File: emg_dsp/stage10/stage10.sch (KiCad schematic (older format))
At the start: 210 parts, among them U1 RS232_CON, U10 EN_VDD, U11 USBLC6, U12 ABM10XTAL-24, U13 BF527, U14 MIC5365, U15 SST25VF040B, U16 ADSP_JTAG_CON, U17 LAN8710A, U18 74LCX541, U19 SFE-MAGJACK, U2 VEE, U20 MAX6711Z, U21 TESTCON, U22 74LCX541, U23 74LCX541, U24 NRF24L01-BREAK, U25 NRF24L01-BREAK, U26 NRF24L01-BREAK, U3 ADM3202, U4 TPS62410, U5 GT12MABE, U6 FCI_USB_B, U7 MT48LC16M16A2, U8 EN_VCC, U9 ABM10XTAL-25

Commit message: working on new (final?) headstage/bridge. added power-over-ethernet to the bridge, as well as programming and debug for the headstage. want to put an LCD on there too...
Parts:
- removed R38, R39: 200, 0402, symbol R
- removed TP38, TP39, TP40, TP41: TP, 2.9mm_hole, symbol TP
- removed TP5: TWI_SCL, TP, symbol TP
- removed TP6: TWI_SDA, TP, symbol TP
- removed U19: SFE-MAGJACK, SFE-MAGJACK, symbol SFE-MAGJACK
- added C?: 100pf, 0402, symbol C
- added C?: 0.1uf, 0402, symbol C
- added C? (x2): 1uf, 0402, symbol C
- added R?: 130, 0402, symbol R
- added R? (x3): 200, 0402, symbol R
- added R? (x4): 10k, 0402, symbol R
- added U?: POE-JACK, POE-JACK, symbol POE-JACK
- added U?: TESTCON, 7x100mil, symbol TESTCON
- added U?: 74LCX541, TSSOP-20, symbol 74LCX541
- added U? (x2): 9X100, omnetics_9, symbol 9X100
- added U?: ADSP_JTAG_CON, 7x2x100, symbol ADSP_JTAG_CON
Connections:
- net labels added: VBUS
- wire segments 570 -> 636
- no-connect marks 25 -> 30
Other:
- note added: "MISO"
- note added: "MOSI"
- note added: "MR"
- note added: "PF2"
- note added: "SCK"
- note added: "TCK"
- note added: "TDI"
- note added: "TDO"
- note added: "TMS"
- note added: "_emu"
- note added: "_trst"
- note added: "this for debugging the headstage."
- note added: "this for programming the headstage."
- moved on the sheet: C48

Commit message: word, schematics for 9/10 are close to done. start changing the boards...
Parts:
- removed D10, D11, D12, D13, D14, D15, D16, D2, D3, D4, D5, D6, D7, D8, D9: LED, 0603, symbol LED
- removed R? (x2): 10k, 0402, symbol R
- added C74, C77: 47pf, 0402, symbol C
- added C91: 1uf, 0402, symbol C
- added D22, D23, D24, D25, D26, D27, D28, D29, D30, D31, D32, D33, D34, D35, D36: 475-2558, D0603, symbol LED
- added R132, R133: 33, 0402, symbol R
- added U42: NHD-0216KZW, NHD-0216KZW, symbol NHD-0216KZW
- D1: value LED -> 475-2558; footprint 0603 -> D0603
- R113: renamed from R?; value 10k -> 22k
- R57, R58, R59, R60, R61, R62, R63, R64, R65, R66, R67, R68, R69, R70, R71, R72: value 130 -> 200
- TP11: value NRF_CSN -> PF0-DR0PRI
- TP12: value NRF_CE -> PF7-DR0SEC
- TP13: value NRF_IRQ -> PF1-RFS0
- TP14: value WIRED_STEP -> PF2-RSCLK
- gave numbers to parts that had none: 15
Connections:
- net GND: now also C74.2, C77.2, C91.1, U42.1 (Vss), U42.10 (DB3), U42.11 (DB4), U42.15 (NC), U42.3 (NC), U42.4 (RS), U42.5 (R/W), U42.6 (E), U42.7 (DB0), U42.8 (DB1), U42.9 (DB2)
- net VDD: now also C91.2, U42.2 (Vdd)
- net at TP18.1, U23.15 (Y4): now also D28.1 (A)
- net at R64.1: now also D28.2 (K)
- net at TP21.1, U23.12 (Y7): now also D34.1 (A)
- net at R70.1: now also D34.2 (K)
- net at TP22.1, U23.11 (Y8): now also D36.1 (A)
- net at R72.1: now also D36.2 (K)
- net at TP17.1, U23.16 (Y3): now also D26.1 (A)
- net at TP16.1, U23.17 (Y2): now also D24.1 (A)
- net at TP8.1, U22.17 (Y2): now also D23.1 (A)
- net at TP9.1, U22.16 (Y3): now also D25.1 (A)
- net at TP10.1, U22.15 (Y4): now also D27.1 (A)
- net at TP11.1, U22.14 (Y5): now also D29.1 (A)
- net at TP12.1, U22.13 (Y6): now also D31.1 (A)
- net at TP14.1, U22.11 (Y8): now also D35.1 (A)
- net at R71.1: now also D35.2 (K)
- net at R67.1: now also D31.2 (K)
- net at R65.1: now also D29.2 (K)
- net at R63.1: now also D27.2 (K)
- net LCD_SDI: now reaches U13.J1 (PG11)
- net LCD_SDI: now also U42.14 (SDI)
- net at U13.J2 (PG12): now also R133.1
- net at U13.K1 (PG9-TACI5): now also R132.1
- net LCD_SDO: now reaches U13.K2 (PG10-TACI6)
- net LCD_SDO: now also U42.13 (SDO)
- net at U18.2 (A1), U21.3 (_cs): now also C77.1
- net at TP15.1, U23.18 (Y1): now also D22.1 (A)
- net at R58.1: now also D22.2 (K)
- net at R60.1: now also D24.2 (K)
- net at R62.1: now also D26.2 (K)
- net at TP20.1, U23.13 (Y6): now also D32.1 (A)
- net at TP19.1, U23.14 (Y5): now also D30.1 (A)
- net at R66.1: now also D30.2 (K)
- net at R68.1: now also D32.2 (K)
- net at TP13.1, U22.12 (Y7): now also D33.1 (A)
- net at R69.1: now also D33.2 (K)
- net at R61.1: now also D25.2 (K)
- net at R59.1: now also D23.2 (K)
- net at U33.2 (A1), U35.3 (_cs): now also C74.1
- new net LCD_CS: R133.2, U42.16 (_cs)
- new net LCD_SCL: R132.2, U42.12 (SCL)
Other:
- note added: "emu pulled hi\ntrst pulled low\non 'stage"
- moved on the sheet: C55, C56, D1, R42, R43, R44, R45, R46, R47, R48, R49, R57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

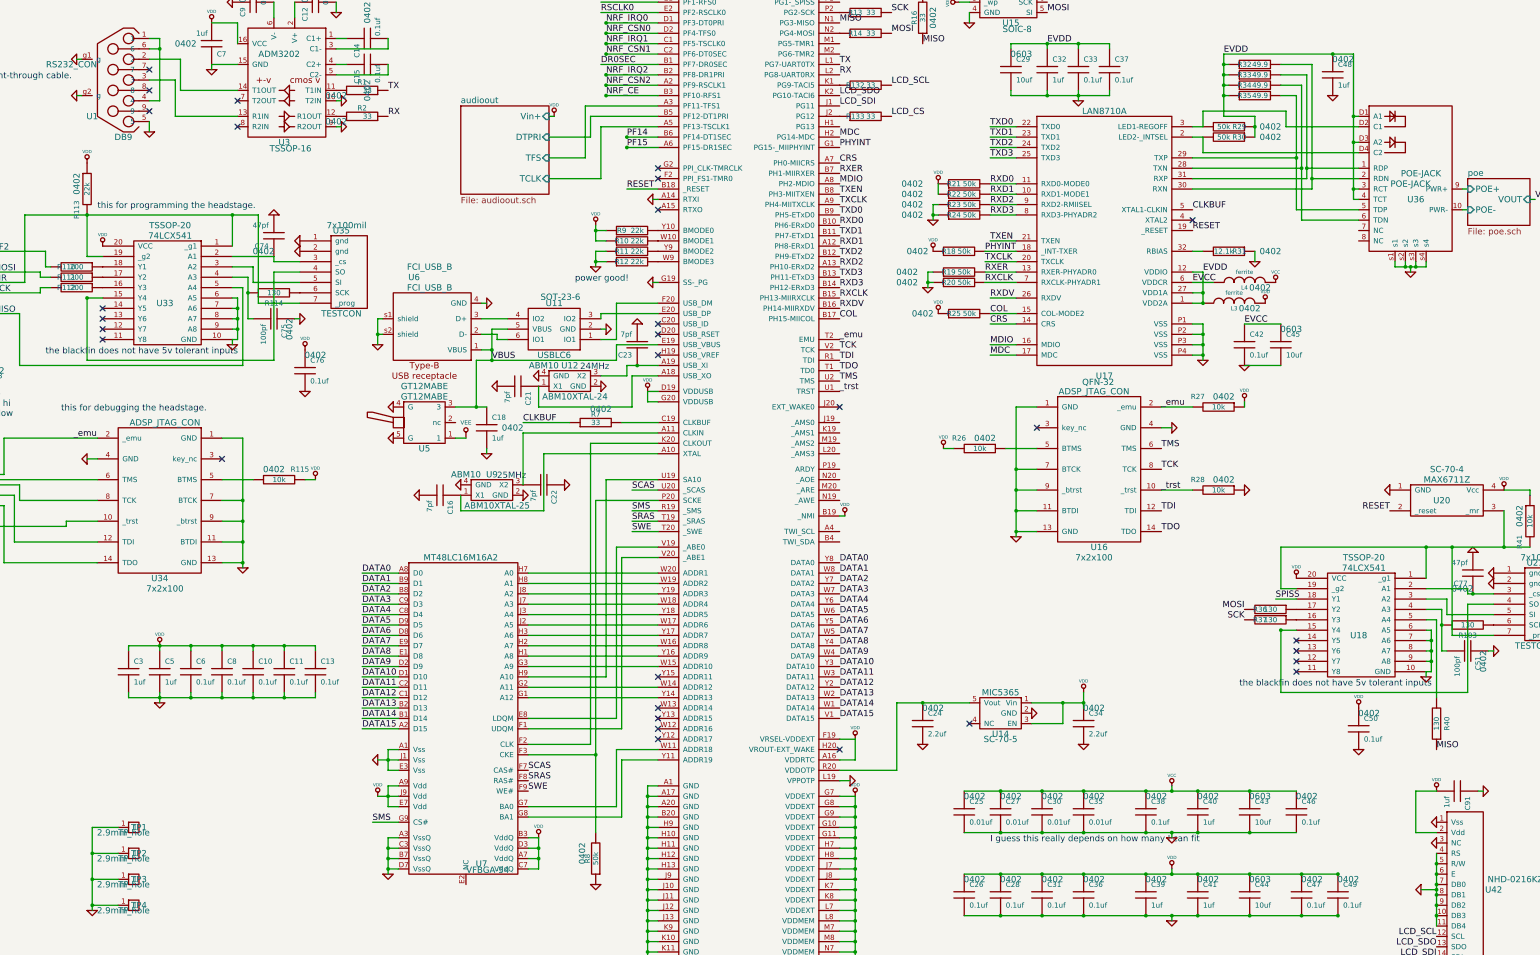
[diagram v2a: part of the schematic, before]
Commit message: working on board layout for stage10 .. time for the checks!
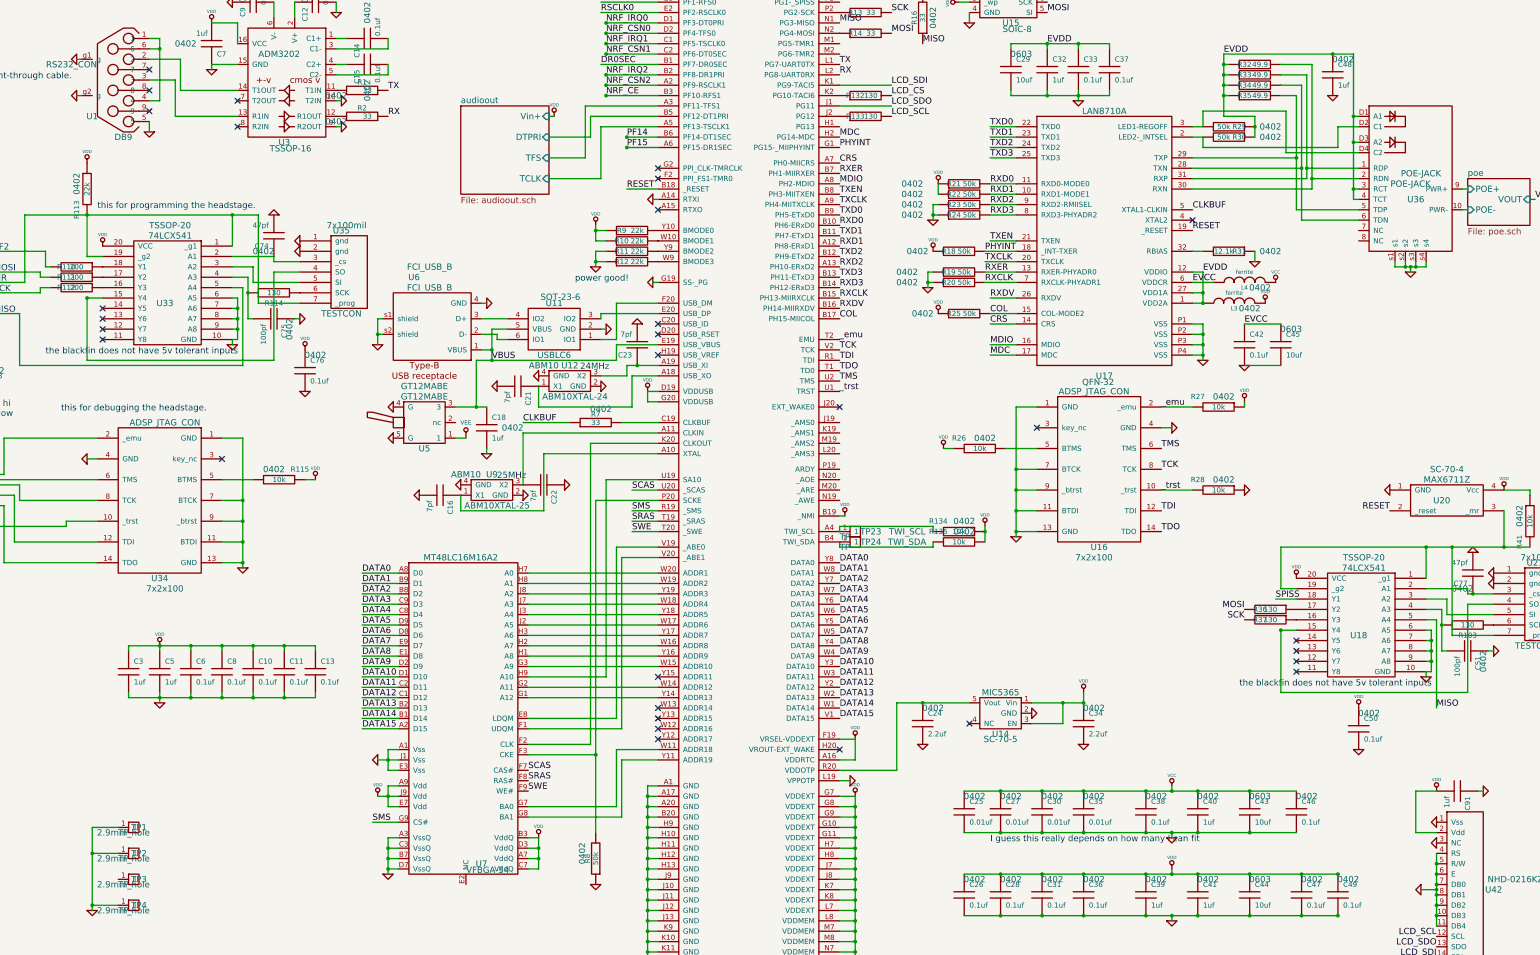
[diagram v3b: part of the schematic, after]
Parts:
- removed R40: 130, 0402, symbol R
- added R134, R135: 10k, 0402, symbol R
- added TP23: TWI_SCL, TP, symbol TP
- added TP24: TWI_SDA, TP, symbol TP
- R132, R133: value 33 -> 130
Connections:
- net GND: no longer TP3.1
- net LCD_CS: now also R132.2; no longer R133.2
- net LCD_SCL: now also R133.2; no longer R132.2
- net LCD_SDI: now also U13.K1 (PG9-TACI5); no longer U13.J1 (PG11)
- net LCD_SDO: now also U13.J1 (PG11); no longer U13.K2 (PG10-TACI6)
- net MISO: now also U18.5 (A4)
- net VDD: now also R134.1, R135.1
- net _emu: no longer U31.8, U34.2 (_emu)
- net at R30.2, U17.2 (LED2-_INTSEL): now also U36.D2 (C1); no longer U36.D4 (C2)
- net at R29.2, U17.3 (LED1-REGOFF): now also U36.D4 (C2); no longer U36.D2 (C1)
- net at U13.A4 (TWI_SCL): now also R134.2, TP23.1
- net at U13.B4 (TWI_SDA): now also R135.2, TP24.1
- net at R132.1: now also U13.K2 (PG10-TACI6); no longer U13.K1 (PG9-TACI5)
- new net: U31.8, U34.2 (_emu)
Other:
- moved on the sheet: R132

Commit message: okay, gerbers are done -- will submit order!
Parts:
- U36: value POE-JACK -> A99645
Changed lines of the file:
@@
-EESchema Schematic File Version 2  date Wed 12 Oct 2011 06:08:50 PM EDT
+EESchema Schematic File Version 2  date Thu 20 Oct 2011 05:59:00 PM EDT
 LIBS:power
 LIBS:device
@@
 Sheet 1 3
 Title "Stage 4 / Copyright 2010 Timothy L Hanson "
-Date "12 oct 2011"
+Date "20 oct 2011"
 Rev ""
 Comp "This design is free: redistribute or modify under the GPL v. 3 or later"
@@
 P 14000 2500
 F 0 "U36" H 14050 2350 60  0000 C CNN
-F 1 "POE-JACK" H 14100 2600 60  0000 C CNN
+F 1 "A99645" H 14100 2600 60  0000 C CNN
 F 2 "POE-JACK" H 14000 2500 60  0000 C CNN
 	1    14000 2500

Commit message: finished parts order to digi-key. not much to do now but wait and/or build up an old board..
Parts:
- U14: value MIC5365 -> MIC5365-2.5
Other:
- note added: "this is for 2.5V, but has a timeout of 140ms,\nso should be ok."
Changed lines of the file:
@@
-EESchema Schematic File Version 2  date Thu 20 Oct 2011 05:59:00 PM EDT
+EESchema Schematic File Version 2  date Sat 22 Oct 2011 02:30:34 PM EDT
 LIBS:power
 LIBS:device
@@
 Sheet 1 3
 Title "Stage 4 / Copyright 2010 Timothy L Hanson "
-Date "20 oct 2011"
+Date "22 oct 2011"
 Rev ""
 Comp "This design is free: redistribute or modify under the GPL v. 3 or later"
@@
 Comment4 ""
 $EndDescr
+Text Notes 13350 5100 0    60   ~ 0
+this is for 2.5V, but has a timeout of 140ms,\nso should be ok.
 Wire Wire Line
 	8500 1750 9000 1750
@@
 P 10050 7600
 F 0 "U14" H 10050 7400 60  0000 C CNN
-F 1 "MIC5365" H 10050 7800 60  0000 C CNN
+F 1 "MIC5365-2.5" H 10050 7800 60  0000 C CNN
 F 2 "SC-70-5" H 10050 7350 60  0000 C CNN
 	1    10050 7600
